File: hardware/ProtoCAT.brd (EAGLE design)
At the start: 59.7 x 53.3 mm, 53 parts, among them U1 ARDUINO

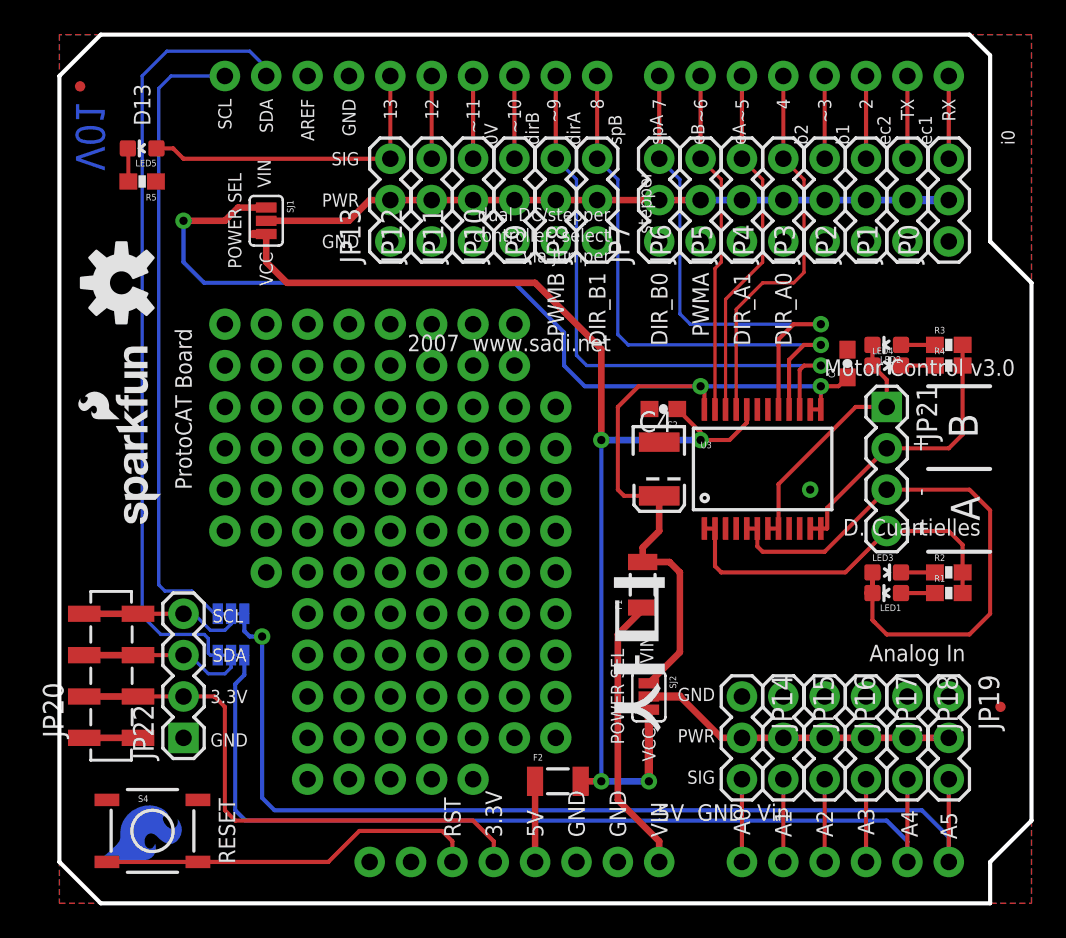
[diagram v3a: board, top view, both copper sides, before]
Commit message: Moved 4 pin SMD headers to Motor Driver
Tied STDBY pin on motor driver to Vcc, added 4 pin SMD header to motor
Driver output, and changed 3-pin headers to locking headers
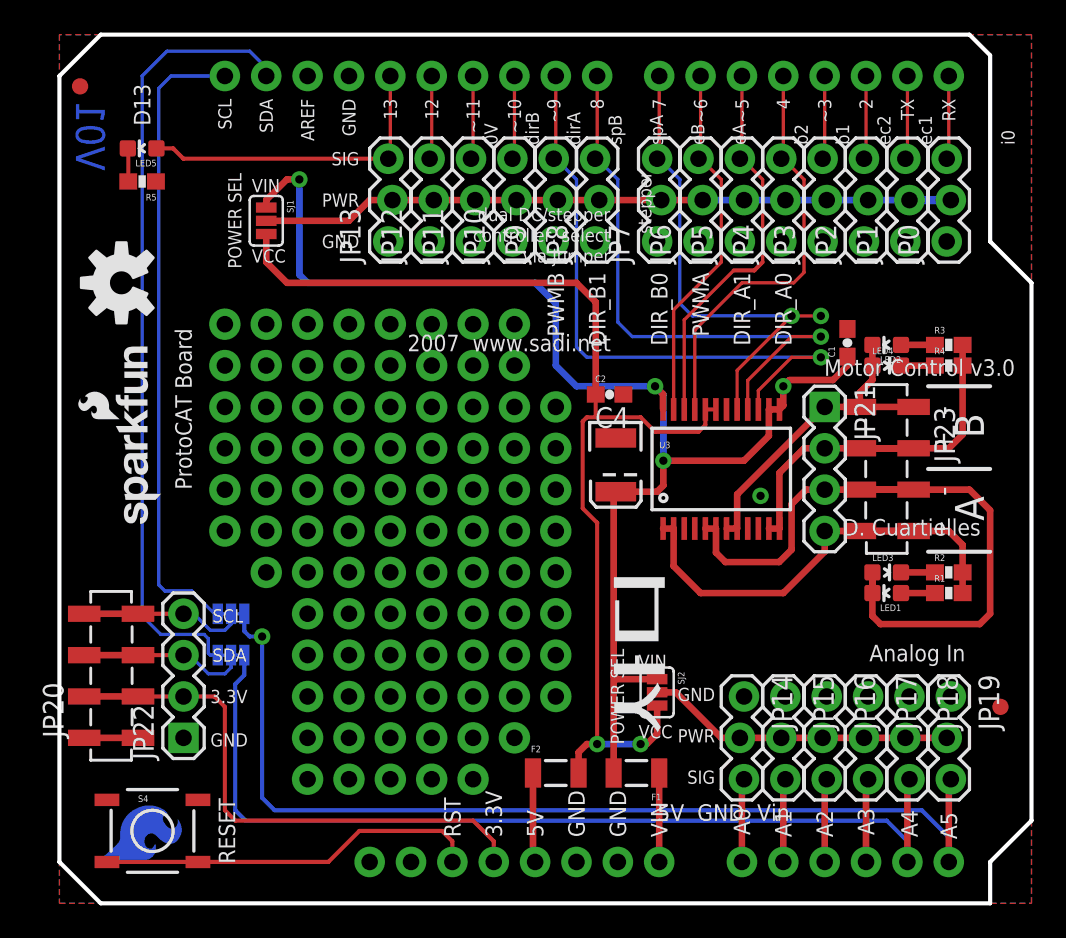
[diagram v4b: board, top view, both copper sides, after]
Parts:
- added JP23: (no value), SparkFun-Connectors:1X04_SMD_STRAIGHT_COMBO
- FID1, FID2: value FIDUCIALUFIDUCIAL -> FIDUCIAL1X2; device SparkFun-Aesthetics:MICRO-FIDUCIAL -> SparkFun-Aesthetics:FIDUCIAL-1X2
- JP0, JP1, JP10, JP11, JP12, JP13, JP14, JP15, JP16, JP17, JP18, JP19, JP2, JP3, JP4, JP5, JP6, JP7, JP8, JP9: device SparkFun-Connectors:1X03 -> SparkFun-Connectors:1X03_LOCK
- U3: value (none) -> TB6612FNG
- moved F1 11.6 mm to (35.4, 8.00), turned to 180 degrees
- moved U$1 5.24 mm to (40.6, 19.1), flipped to the top, turned to 270 degrees
- moved JP21 3.81 mm to (47.0, 30.5)
- moved C2 3.42 mm to (33.8, 31.2), turned to 0 degrees
- moved C4 2.68 mm to (34.2, 26.9)
- moved U3 2.54 mm to (40.6, 26.7)
- moved C1 1.27 mm to (48.4, 34.4)
- moved SJ2 0.57 mm to (36.7, 13.0)
- moved F2 0.52 mm to (30.5, 8.00)
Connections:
- net BIN2 renamed N$20
- removed net STBY: U3.19
- net AOUT1: now also JP23.4
- net AOUT2: now also JP23.3
- net BOUT1: now also JP23.2
- net BOUT2: now also JP23.1
- net FUSED_VCC: now also U3.19
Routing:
- net VIN: track 17.3 -> 5.46 mm
- net FUSED_VCC: track 73.4 -> 68.3 mm, vias 4 -> 2
- net AOUT1: track 23.0 -> 27.3 mm
- net AOUT2: track 37.1 -> 41.2 mm
- net BOUT1: track 18.0 -> 21.8 mm
- net FUSED_VIN: track 85.4 -> 82.8 mm, vias 3 -> 4
- net AIN1: track 23.8 -> 25.8 mm
- net AIN2: track 21.9 -> 23.9 mm
- net PWMB: track 36.8 -> 38.5 mm
- net N$20: track 34.5 -> 36.0 mm
- net PWMA: track 21.2 -> 22.4 mm
- net BIN1: track 31.3 -> 30.8 mm, vias 1 -> 2
- net VCC: track 4.95 -> 5.51 mm
- net ANALOG_PWR_RAIL: track 19.5 -> 18.9 mm

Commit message: Removed unused layers on board
Removed unused middle layers of board and cleaned up silkscreen artwork
on Ludus Logo
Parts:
- moved U$1 6.35 mm to (40.6, 25.4)
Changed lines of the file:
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@@
 <layers>
 <layer number="1" name="Top" color="4" fill="1" visible="yes" active="yes"/>
-<layer number="2" name="Route2" color="1" fill="3" visible="no" active="yes"/>
-<layer number="15" name="Route15" color="4" fill="6" visible="no" active="yes"/>
 <layer number="16" name="Bottom" color="1" fill="1" visible="yes" active="yes"/>
 <layer number="17" name="Pads" color="2" fill="1" visible="yes" active="yes"/>
@@
 <element name="SJ3" library="SparkFun-Passives" package="PAD-JUMPER-3-3OF3_NC_BY_TRACE_YES_SILK_FULL_BOX" value="" x="10.541" y="15.24" rot="MR180"/>
 <element name="SJ4" library="SparkFun-Passives" package="PAD-JUMPER-3-3OF3_NC_BY_TRACE_YES_SILK_FULL_BOX" value="" x="10.541" y="17.78" rot="MR180"/>
-<element name="U$1" library="SparkFun-Aesthetics" package="SFE_LUDUS-M" value="SFE_LUDUS" x="40.64" y="19.05" rot="R270"/>
+<element name="U$1" library="SparkFun-Aesthetics" package="SFE_LUDUS-M" value="SFE_LUDUS" x="40.64" y="25.4" rot="R270"/>
 <element name="LOGO3" library="SparkFun-Aesthetics" package="SFE_LOGO_FLAME_COPPER_.2" value="SFE_LOGO_FLAME.2COP" x="2.159" y="2.286" rot="SMR90"/>
 <element name="LOGO4" library="SparkFun-Aesthetics" package="SFE_LOGO_NAME_FLAME_.1" value="SFE_LOGO_NAME_FLAME.1_INCH" x="53.34" y="19.05" rot="MR90"/>

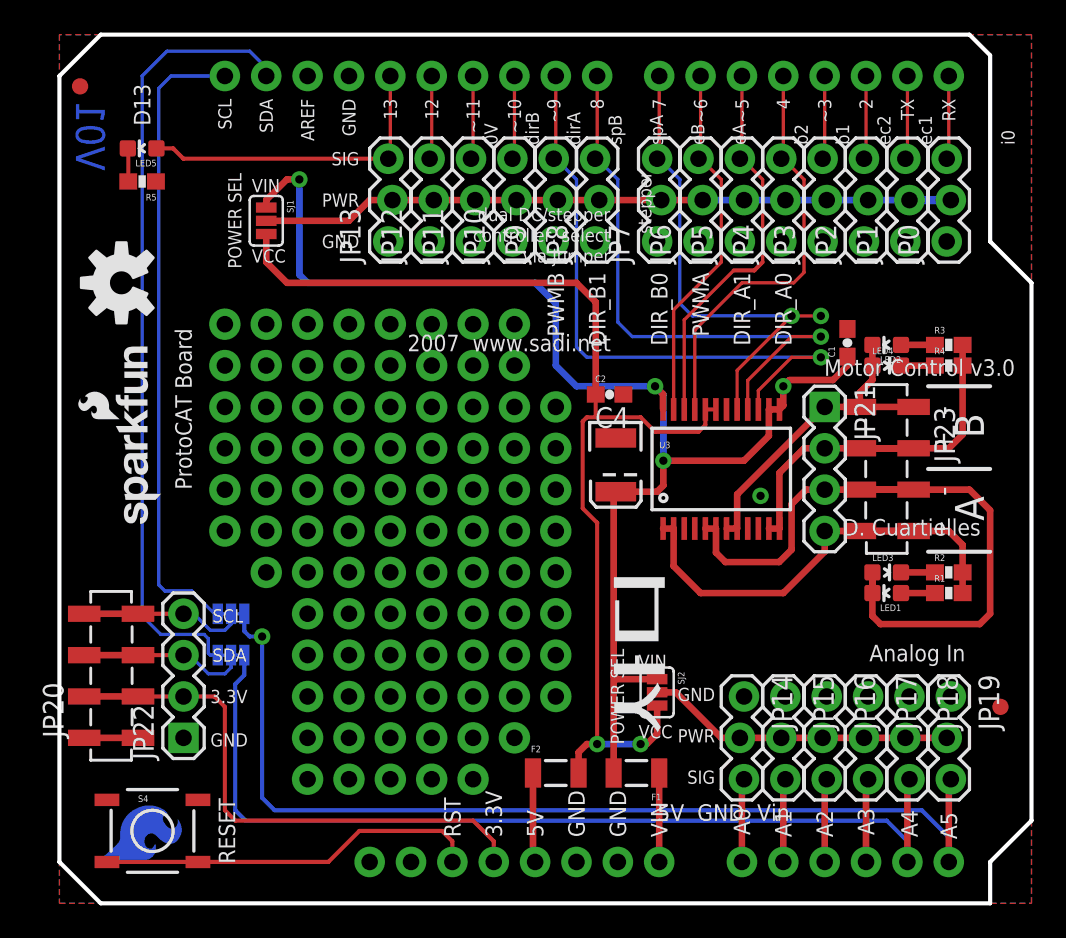
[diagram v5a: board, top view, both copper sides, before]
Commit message: Final board changes -- ready for reds
Moved I2C header down to account for panelizer, moved a the cut jumpers
for A4/A5 & SCL/SDA on bottom trace
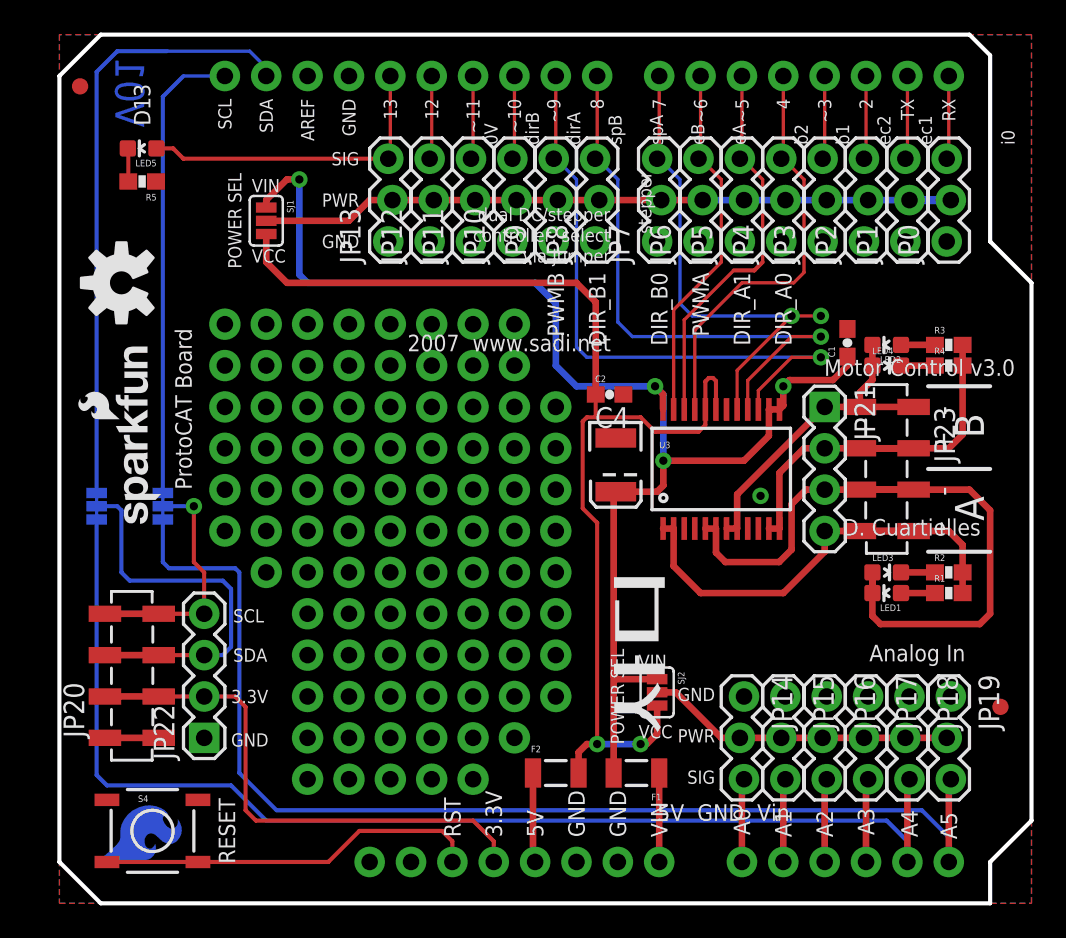
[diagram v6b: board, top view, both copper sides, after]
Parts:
- moved SJ3 12.3 mm to (2.29, 24.4), turned to 270 degrees
- moved SJ4 7.82 mm to (6.35, 24.4), turned to 270 degrees
- moved JP20 1.27 mm to (4.45, 10.2)
- moved JP22 1.27 mm to (8.89, 10.2)
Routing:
- net A4: track 58.2 -> 73.6 mm
- net SDA_I2C_PORT: track 7.11 -> 20.8 mm
- net SDA: track 48.5 -> 37.7 mm
- net SCL: track 39.2 -> 28.7 mm
- net A5: track 62.0 -> 71.7 mm, vias 1 -> 0
- net SCL_I2C_PORT: track 10.2 -> 14.9 mm, vias 0 -> 1
- net FUSED_VCC: track 68.3 -> 72.0 mm
- net 3.3V: track 33.8 -> 32.5 mm
